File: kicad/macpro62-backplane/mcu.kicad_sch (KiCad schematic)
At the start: 1 part

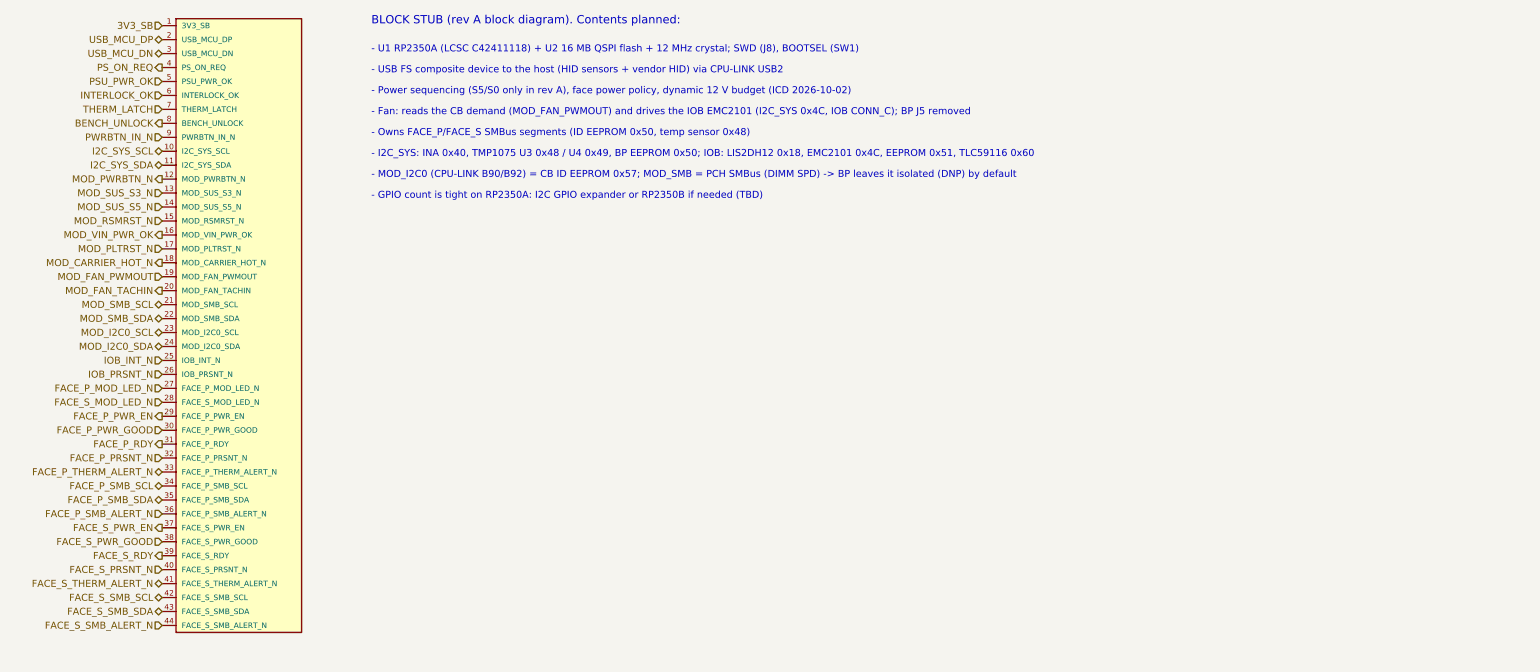
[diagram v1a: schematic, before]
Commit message: ICD rev 2: 45 deg faces, 445 W ceiling + live power target (INA228 telemetry), ribbon MCIO jog cables, BT on S0, fan fail-safe, port-module I2C map
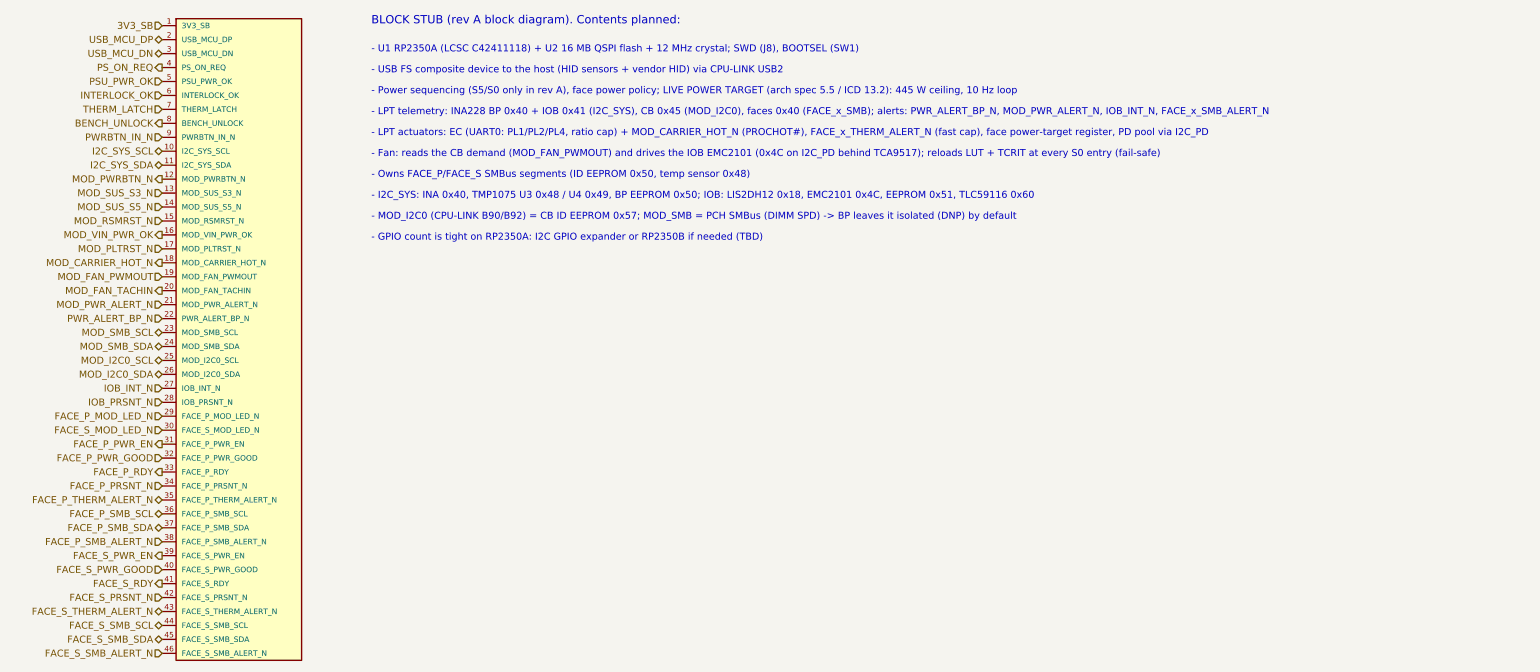
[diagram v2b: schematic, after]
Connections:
- net FACE_P_MOD_LED_N: now also #BLK2.29 (FACE_P_MOD_LED_N); no longer #BLK2.27 (FACE_P_MOD_LED_N)
- net FACE_P_PRSNT_N: now also #BLK2.34 (FACE_P_PRSNT_N); no longer #BLK2.32 (FACE_P_PRSNT_N)
- net FACE_P_PWR_EN: now also #BLK2.31 (FACE_P_PWR_EN); no longer #BLK2.29 (FACE_P_PWR_EN)
- net FACE_P_PWR_GOOD: now also #BLK2.32 (FACE_P_PWR_GOOD); no longer #BLK2.30 (FACE_P_PWR_GOOD)
- net FACE_P_RDY: now also #BLK2.33 (FACE_P_RDY); no longer #BLK2.31 (FACE_P_RDY)
- net FACE_P_SMB_ALERT_N: now also #BLK2.38 (FACE_P_SMB_ALERT_N); no longer #BLK2.36 (FACE_P_SMB_ALERT_N)
- net FACE_P_SMB_SCL: now also #BLK2.36 (FACE_P_SMB_SCL); no longer #BLK2.34 (FACE_P_SMB_SCL)
- net FACE_P_SMB_SDA: now also #BLK2.37 (FACE_P_SMB_SDA); no longer #BLK2.35 (FACE_P_SMB_SDA)
- net FACE_P_THERM_ALERT_N: now also #BLK2.35 (FACE_P_THERM_ALERT_N); no longer #BLK2.33 (FACE_P_THERM_ALERT_N)
- net FACE_S_MOD_LED_N: now also #BLK2.30 (FACE_S_MOD_LED_N); no longer #BLK2.28 (FACE_S_MOD_LED_N)
- net FACE_S_PRSNT_N: now also #BLK2.42 (FACE_S_PRSNT_N); no longer #BLK2.40 (FACE_S_PRSNT_N)
- net FACE_S_PWR_EN: now also #BLK2.39 (FACE_S_PWR_EN); no longer #BLK2.37 (FACE_S_PWR_EN)
- net FACE_S_PWR_GOOD: now also #BLK2.40 (FACE_S_PWR_GOOD); no longer #BLK2.38 (FACE_S_PWR_GOOD)
- net FACE_S_RDY: now also #BLK2.41 (FACE_S_RDY); no longer #BLK2.39 (FACE_S_RDY)
- net FACE_S_SMB_ALERT_N: now also #BLK2.46 (FACE_S_SMB_ALERT_N); no longer #BLK2.44 (FACE_S_SMB_ALERT_N)
- net FACE_S_SMB_SCL: now also #BLK2.44 (FACE_S_SMB_SCL); no longer #BLK2.42 (FACE_S_SMB_SCL)
- net FACE_S_SMB_SDA: now also #BLK2.45 (FACE_S_SMB_SDA); no longer #BLK2.43 (FACE_S_SMB_SDA)
- net FACE_S_THERM_ALERT_N: now also #BLK2.43 (FACE_S_THERM_ALERT_N); no longer #BLK2.41 (FACE_S_THERM_ALERT_N)
- net IOB_INT_N: now also #BLK2.27 (IOB_INT_N); no longer #BLK2.25 (IOB_INT_N)
- net IOB_PRSNT_N: now also #BLK2.28 (IOB_PRSNT_N); no longer #BLK2.26 (IOB_PRSNT_N)
- net MOD_I2C0_SCL: now also #BLK2.25 (MOD_I2C0_SCL); no longer #BLK2.23 (MOD_I2C0_SCL)
- net MOD_I2C0_SDA: now also #BLK2.26 (MOD_I2C0_SDA); no longer #BLK2.24 (MOD_I2C0_SDA)
- net MOD_SMB_SCL: now also #BLK2.23 (MOD_SMB_SCL); no longer #BLK2.21 (MOD_SMB_SCL)
- net MOD_SMB_SDA: now also #BLK2.24 (MOD_SMB_SDA); no longer #BLK2.22 (MOD_SMB_SDA)
- new net MOD_PWR_ALERT_N: #BLK2.21 (MOD_PWR_ALERT_N)
- new net PWR_ALERT_BP_N: #BLK2.22 (PWR_ALERT_BP_N)
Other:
- note added: "- Fan: reads the CB demand (MOD_FAN_PWMOUT) and drives the IOB EMC2101 (0x4C on I2C_PD behind TCA9517); reloads LUT + TCRIT at every S0 entry (fail-safe)"
- note added: "- LPT actuators: EC (UART0: PL1/PL2/PL4, ratio cap) + MOD_CARRIER_HOT_N (PROCHOT#), FACE_x_THERM_ALERT_N (fast cap), face power-target register, PD pool via I2C_PD"
- note added: "- LPT telemetry: INA228 BP 0x40 + IOB 0x41 (I2C_SYS), CB 0x45 (MOD_I2C0), faces 0x40 (FACE_x_SMB); alerts: PWR_ALERT_BP_N, MOD_PWR_ALERT_N, IOB_INT_N, FACE_x_SMB_ALERT_N"
- note added: "- Power sequencing (S5/S0 only in rev A), face power policy; LIVE POWER TARGET (arch spec 5.5 / ICD 13.2): 445 W ceiling, 10 Hz loop"
- note removed: "- Fan: reads the CB demand (MOD_FAN_PWMOUT) and drives the IOB EMC2101 (I2C_SYS 0x4C, IOB CONN_C); BP J5 removed"
- note removed: "- Power sequencing (S5/S0 only in rev A), face power policy, dynamic 12 V budget (ICD 2026-10-02)"
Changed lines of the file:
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@@
+		(effects (font (size 1.27 1.27)) (justify right))
+	)
+	(hierarchical_label "MOD_PWR_ALERT_N"
+		(shape input)
+		(at 38.1 81.28 180)
+		(effects (font (size 1.27 1.27)) (justify right))
+	)
+	(hierarchical_label "PWR_ALERT_BP_N"
+		(shape input)
+		(at 38.1 83.82 180)
 		(effects (font (size 1.27 1.27)) (justify right))
 	)
 	(hierarchical_label "MOD_SMB_SCL"
 		(shape bidirectional)
-		(at 38.1 81.28 180)
+		(at 38.1 86.36 180)
 		(effects (font (size 1.27 1.27)) (justify right))
 	)
 	(hierarchical_label "MOD_SMB_SDA"
 		(shape bidirectional)
-		(at 38.1 83.82 180)
+		(at 38.1 88.90 180)
 		(effects (font (size 1.27 1.27)) (justify right))
 	)
 	(hierarchical_label "MOD_I2C0_SCL"
 		(shape bidirectional)
-		(at 38.1 86.36 180)
+		(at 38.1 91.44 180)
 		(effects (font (size 1.27 1.27)) (justify right))
 	)
 	(hierarchical_label "MOD_I2C0_SDA"
 		(shape bidirectional)
-		(at 38.1 88.90 180)
+		(at 38.1 93.98 180)
 		(effects (font (size 1.27 1.27)) (justify right))
 	)
 	(hierarchical_label "IOB_INT_N"
 		(shape input)
-		(at 38.1 91.44 180)
+		(at 38.1 96.52 180)
 		(effects (font (size 1.27 1.27)) (justify right))
 	)
 	(hierarchical_label "IOB_PRSNT_N"
 		(shape input)
-		(at 38.1 93.98 180)
+		(at 38.1 99.06 180)
 		(effects (font (size 1.27 1.27)) (justify right))
 	)
 	(hierarchical_label "FACE_P_MOD_LED_N"
 		(shape input)
-		(at 38.1 96.52 180)
+		(at 38.1 101.60 180)
 		(effects (font (size 1.27 1.27)) (justify right))
 	)
 	(hierarchical_label "FACE_S_MOD_LED_N"
 		(shape input)
-		(at 38.1 99.06 180)
+		(at 38.1 104.14 180)
 		(effects (font (size 1.27 1.27)) (justify right))
 	)
 	(hierarchical_label "FACE_P_PWR_EN"
 		(shape output)
-		(at 38.1 101.60 180)
+		(at 38.1 106.68 180)
 		(effects (font (size 1.27 1.27)) (justify right))
 	)
 	(hierarchical_label "FACE_P_PWR_GOOD"
 		(shape input)
-		(at 38.1 104.14 180)
+		(at 38.1 109.22 180)
 		(effects (font (size 1.27 1.27)) (justify right))
 	)
 	(hierarchical_label "FACE_P_RDY"
 		(shape output)
-		(at 38.1 106.68 180)
+		(at 38.1 111.76 180)
 		(effects (font (size 1.27 1.27)) (justify right))
 	)
 	(hierarchical_label "FACE_P_PRSNT_N"
 		(shape input)
-		(at 38.1 109.22 180)
+		(at 38.1 114.30 180)
 		(effects (font (size 1.27 1.27)) (justify right))
 	)
 	(hierarchical_label "FACE_P_THERM_ALERT_N"
 		(shape bidirectional)
-		(at 38.1 111.76 180)
+		(at 38.1 116.84 180)
 		(effects (font (size 1.27 1.27)) (justify right))
 	)
 	(hierarchical_label "FACE_P_SMB_SCL"
 		(shape bidirectional)
-		(at 38.1 114.30 180)
+		(at 38.1 119.38 180)
 		(effects (font (size 1.27 1.27)) (justify right))
 	)
 	(hierarchical_label "FACE_P_SMB_SDA"
 		(shape bidirectional)
-		(at 38.1 116.84 180)
+		(at 38.1 121.92 180)
 		(effects (font (size 1.27 1.27)) (justify right))
 	)
 	(hierarchical_label "FACE_P_SMB_ALERT_N"
 		(shape input)
-		(at 38.1 119.38 180)
+		(at 38.1 124.46 180)
 		(effects (font (size 1.27 1.27)) (justify right))
 	)
 	(hierarchical_label "FACE_S_PWR_EN"
 		(shape output)
-		(at 38.1 121.92 180)
+		(at 38.1 127.00 180)
 		(effects (font (size 1.27 1.27)) (justify right))
 	)
 	(hierarchical_label "FACE_S_PWR_GOOD"
 		(shape input)
-		(at 38.1 124.46 180)
+		(at 38.1 129.54 180)
 		(effects (font (size 1.27 1.27)) (justify right))
 	)
 	(hierarchical_label "FACE_S_RDY"
 		(shape output)
-		(at 38.1 127.00 180)
+		(at 38.1 132.08 180)
 		(effects (font (size 1.27 1.27)) (justify right))
 	)
 	(hierarchical_label "FACE_S_PRSNT_N"
 		(shape input)
-		(at 38.1 129.54 180)
+		(at 38.1 134.62 180)
 		(effects (font (size 1.27 1.27)) (justify right))
 	)
 	(hierarchical_label "FACE_S_THERM_ALERT_N"
 		(shape bidirectional)
-		(at 38.1 132.08 180)
+		(at 38.1 137.16 180)
 		(effects (font (size 1.27 1.27)) (justify right))
 	)
 	(hierarchical_label "FACE_S_SMB_SCL"
 		(shape bidirectional)
-		(at 38.1 134.62 180)
+		(at 38.1 139.70 180)
 		(effects (font (size 1.27 1.27)) (justify right))
 	)
 	(hierarchical_label "FACE_S_SMB_SDA"
 		(shape bidirectional)
-		(at 38.1 137.16 180)
+		(at 38.1 142.24 180)
 		(effects (font (size 1.27 1.27)) (justify right))
 	)
 	(hierarchical_label "FACE_S_SMB_ALERT_N"
 		(shape input)
-		(at 38.1 139.70 180)
+		(at 38.1 144.78 180)
 		(effects (font (size 1.27 1.27)) (justify right))
 	)
@@
 		(pin "44"
 		)
+		(pin "45"
+		)
+		(pin "46"
+		)
 		(instances
 			(project "backplane"
-				(path "/6a1c2d3e-0000-4000-8000-000000000062/89d03002-a1b1-4403-bf24-5238af15a71b"
+				(path "/6a1c2d3e-0000-4000-8000-000000000062/f438f003-2154-42c2-869f-bdabceeaef13"
 					(reference "#BLK2")
 					(unit 1)
@@
 		(effects (font (size 1.27 1.27)) (justify left bottom))
 	)
-	(text "- Power sequencing (S5/S0 only in rev A), face power policy, dynamic 12 V budget (ICD 2026-10-02)"
+	(text "- Power sequencing (S5/S0 only in rev A), face power policy; LIVE POWER TARGET (arch spec 5.5 / ICD 13.2): 445 W ceiling, 10 Hz loop"
 		(exclude_from_sim no)
 		(at 76.20 43.18 0)
 		(effects (font (size 1.27 1.27)) (justify left bottom))
 	)
-	(text "- Fan: reads the CB demand (MOD_FAN_PWMOUT) and drives the IOB EMC2101 (I2C_SYS 0x4C, IOB CONN_C); BP J5 removed"
+	(text "- LPT telemetry: INA228 BP 0x40 + IOB 0x41 (I2C_SYS), CB 0x45 (MOD_I2C0), faces 0x40 (FACE_x_SMB); alerts: PWR_ALERT_BP_N, MOD_PWR_ALERT_N, IOB_INT_N, FACE_x_SMB_ALERT_N"
 		(exclude_from_sim no)
 		(at 76.20 46.99 0)
 		(effects (font (size 1.27 1.27)) (justify left bottom))
 	)
+	(text "- LPT actuators: EC (UART0: PL1/PL2/PL4, ratio cap) + MOD_CARRIER_HOT_N (PROCHOT#), FACE_x_THERM_ALERT_N (fast cap), face power-target register, PD pool via I2C_PD"
+		(exclude_from_sim no)
+		(at 76.20 50.80 0)
+		(effects (font (size 1.27 1.27)) (justify left bottom))
+	)
+	(text "- Fan: reads the CB demand (MOD_FAN_PWMOUT) and drives the IOB EMC2101 (0x4C on I2C_PD behind TCA9517); reloads LUT + TCRIT at every S0 entry (fail-safe)"
+		(exclude_from_sim no)
+		(at 76.20 54.61 0)
+		(effects (font (size 1.27 1.27)) (justify left bottom))
+	)
 	(text "- Owns FACE_P/FACE_S SMBus segments (ID EEPROM 0x50, temp sensor 0x48)"
 		(exclude_from_sim no)
-		(at 76.20 50.80 0)
+		(at 76.20 58.42 0)
 		(effects (font (size 1.27 1.27)) (justify left bottom))
 	)
 	(text "- I2C_SYS: INA 0x40, TMP1075 U3 0x48 / U4 0x49, BP EEPROM 0x50; IOB: LIS2DH12 0x18, EMC2101 0x4C, EEPROM 0x51, TLC59116 0x60"
 		(exclude_from_sim no)
-		(at 76.20 54.61 0)
+		(at 76.20 62.23 0)
 		(effects (font (size 1.27 1.27)) (justify left bottom))
 	)
 	(text "- MOD_I2C0 (CPU-LINK B90/B92) = CB ID EEPROM 0x57; MOD_SMB = PCH SMBus (DIMM SPD) -> BP leaves it isolated (DNP) by default"
 		(exclude_from_sim no)
-		(at 76.20 58.42 0)
+		(at 76.20 66.04 0)
 		(effects (font (size 1.27 1.27)) (justify left bottom))
 	)
 	(text "- GPIO count is tight on RP2350A: I2C GPIO expander or RP2350B if needed (TBD)"
 		(exclude_from_sim no)
-		(at 76.20 62.23 0)
-		(effects (font (size 1.27 1.27)) (justify left bottom))
-	)
+		(at 76.20 69.85 0)
+		(effects (font (size 1.27 1.27)) (justify left bottom))
+	)
